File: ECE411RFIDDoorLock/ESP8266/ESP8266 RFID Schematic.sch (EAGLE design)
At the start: 21 parts, among them T1 2N2222, T2 2N2222, X1 ESP-12E

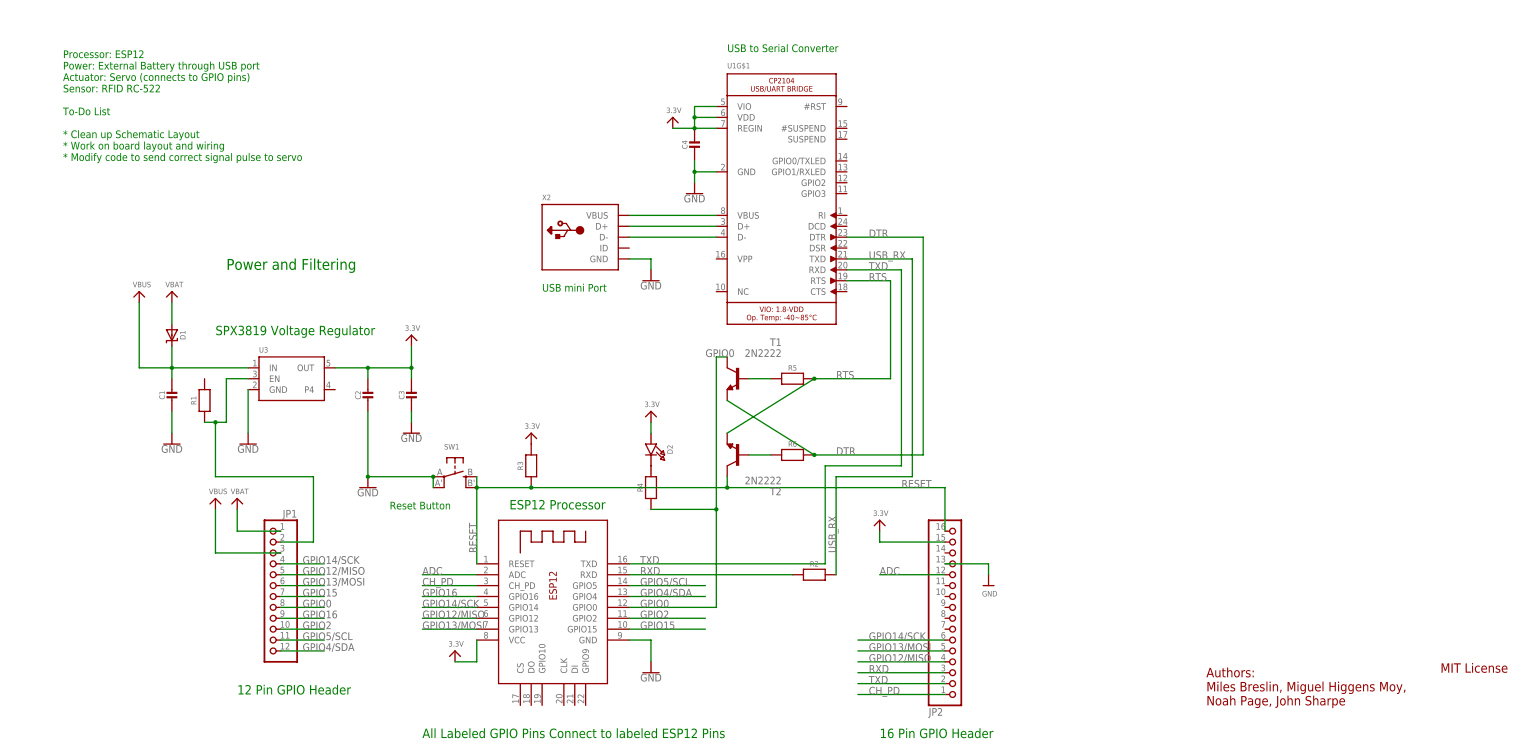
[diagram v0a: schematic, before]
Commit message: Update ESP8266 RFID Schematic.sch
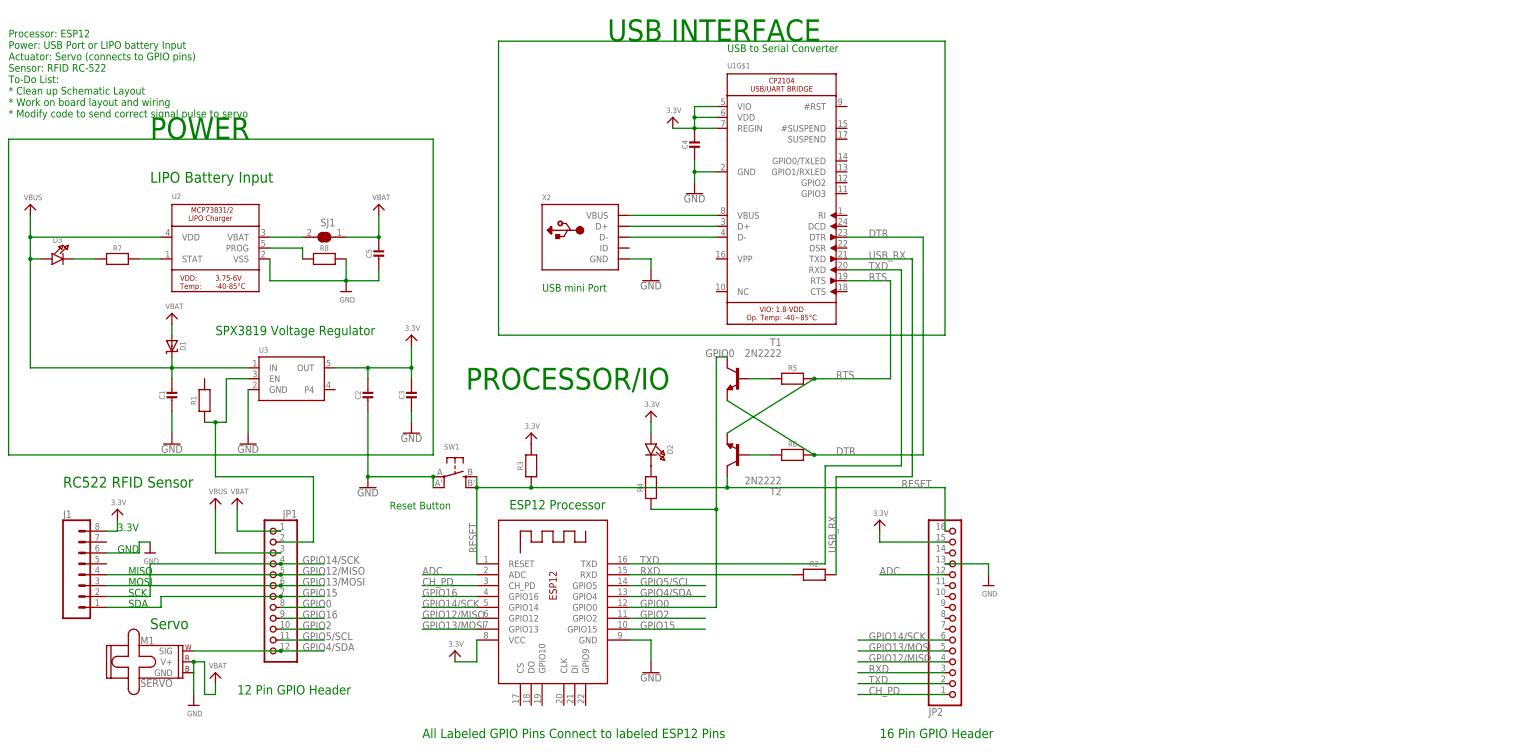
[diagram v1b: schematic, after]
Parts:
- added C5: (no value), microbuilder:CAP_CERAMIC0603MINI
- added D3: (no value), microbuilder:LED0603
- added J1: (no value), SparkFun-Connectors:CONN_08"
- added M1: SERVO, SparkFun-Electromechanical:SERVO
- added R7: (no value), microbuilder:RESISTOR0603MINI
- added R8: (no value), microbuilder:RESISTOR0805_NOOUTLINE
- added SJ1: (no value), microbuilder:SOLDERJUMPER_CLOSED
- added U2: (no value), microbuilder:MCP73831/2
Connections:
- new net N$10: SJ1.2, U2.VBAT
- new net N$11: R8.1, U2.PROG
- new net N$8: D3.C, R7.1
- new net N$9: R7.2, U2.STAT
- net 3.3V: now also J1.8
- net GND: now also C5.2, J1.6, R8.2, U2.VSS
- net GPIO12/MISO: now also J1.4
- net GPIO13/MOSI: now also J1.3
- net GPIO14/SCK: now also J1.2
- net GPIO15: now also J1.1
- net GPIO4/SDA: now also M1.SIG
- net VBAT: now also C5.1, M1.GND, M1.V+, SJ1.1
- net VBUS: now also D3.A, U2.VDD
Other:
- note added: "3.3V"
- note added: "GND"
- note added: "LIPO Battery Input"
- note added: "MISO"
- note added: "MOSI"
- note added: "POWER"
- note added: "PROCESSOR/IO"
- note added: "Processor: ESP12 Power: USB Port or LIPO battery Input Actuator: Servo (connects to GPIO pins) Sensor: RFID RC-522 To-Do List: * Clean up Schematic Layout * Work on board layout and wiring * Modify code to send correct signal pulse to servo"
- note added: "RC522 RFID Sensor"
- note added: "SCK"
- note added: "SDA"
- note added: "Servo"
- note added: "USB INTERFACE"
- note removed: "Authors: Miles Breslin, Miguel Higgens Moy, Noah Page, John Sharpe"
- note removed: "MIT License"
- note removed: "Power and Filtering"
- note removed: "Processor: ESP12 Power: External Battery through USB port Actuator: Servo (connects to GPIO pins) Sensor: RFID RC-522 To-Do List * Clean up Schematic Layout * Work on board layout and wiring * Modify code to send correct signal pulse to servo"
- moved on the sheet: D1

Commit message: First pass at PCB layout
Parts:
- removed C5: (no value), microbuilder:CAP_CERAMIC0603MINI
- removed D1: (no value), microbuilder:DIODE-SCHOTTKYDO-1N4148
- removed D3: (no value), microbuilder:LED0603
- removed JP1: (no value), microbuilder:HEADER-1X12
- removed JP2: (no value), microbuilder:HEADER-1X16
- removed R8: (no value), microbuilder:RESISTOR0805_NOOUTLINE
- removed SJ1: (no value), microbuilder:SOLDERJUMPER_CLOSED
- removed U2: (no value), microbuilder:MCP73831/2
- removed X2: (no value), microbuilder:USBMINIB
- added D4: MBR0540, microbuilder:DIODE-SCHOTTKYSOD-123
- added J2, J3: (no value), SparkFun-Connectors:CONN_02
- added JP4: (no value), microbuilder:HEADER-1X16ROUND
- added JP5: (no value), microbuilder:HEADER-1X12
- added Q3: DMG341, microbuilder:MOSFET-P
- added X4: 20329, microbuilder:USB_MICRO_20329_V2
- C2, C3: value (none) -> 10µF
- R1, R7: value (none) -> 10k
- T1, T2: value 2N2222 -> 600mA/40V; device adafruit:2N2222 -> SparkFun-DiscreteSemi:TRANS_NPN-MMBT2222AL
- U3: value (none) -> AP2112-3.3
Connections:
- removed net N$1: JP1.2, R1.1, U3.EN
- removed net N$11: R8.1, U2.PROG
- removed net OUT: C2.1, C3.1, U3.OUT
- new net EN: JP5.2
- new net N$14: C4.1, U1G$1.VDD, U1G$1.VIO
- net 3.3V: now also C2.1, C3.1, JP4.15, U3.OUT; no longer C4.1, JP2.15, U1G$1.VDD, U1G$1.VIO
- net ADC: now also JP4.12; no longer JP2.12
- net CH_PD: now also JP4.1; no longer JP2.1
- net GND: now also J2.1, J3.1, JP4.13, M1.GND, R7.1, X4.GND; no longer C5.2, JP2.13, R8.2, U2.VSS, X2.GND
- net GPIO0: now also JP5.8; no longer JP1.8
- net GPIO12/MISO: now also JP4.4, JP5.5; no longer JP1.5, JP2.4
- net GPIO13/MOSI: now also JP4.5, JP5.6; no longer JP1.6, JP2.5
- net GPIO14/SCK: now also JP4.6, JP5.4; no longer JP1.4, JP2.6
- net GPIO15: now also JP5.7; no longer JP1.7
- net GPIO16: now also JP5.9; no longer JP1.9
- net GPIO2: now also JP5.10; no longer JP1.10
- net GPIO4/SDA: now also JP5.12; no longer JP1.12
- net GPIO5/SCL: now also J3.2, JP5.11; no longer JP1.11
- net N$10: now also R1.1, U3.EN; no longer SJ1.2, U2.VBAT
- net N$2: now also X4.VBUS; no longer X2.VBUS
- net N$3: now also X4.D+; no longer X2.D+
- net N$4: now also X4.D-; no longer X2.D-
- net N$8: now also C1.1, D4.C, Q3.S, R1.2, U3.IN; no longer D3.C, R7.1
- net N$9: now also D4.A, Q3.G; no longer U2.STAT
- net RESET: now also JP4.16; no longer JP2.16
- net RXD: now also JP4.3; no longer JP2.3
- net TXD: now also JP4.2; no longer JP2.2
- net VBAT: now also J2.2, JP5.1, Q3.D; no longer C5.1, D1.A, JP1.1, M1.GND, SJ1.1
- net VBUS: now also JP5.3; no longer C1.1, D1.C, D3.A, JP1.3, U2.VDD, U3.IN
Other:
- note removed: "12 Pin GPIO Header"
- note removed: "16 Pin GPIO Header"
- note removed: "LIPO Battery Input"
- note removed: "SPX3819 Voltage Regulator"
- note removed: "USB mini Port"
- moved on the sheet: C1, C2, C3, C4, J1, M1, R1, R3, R7, SW1, U3

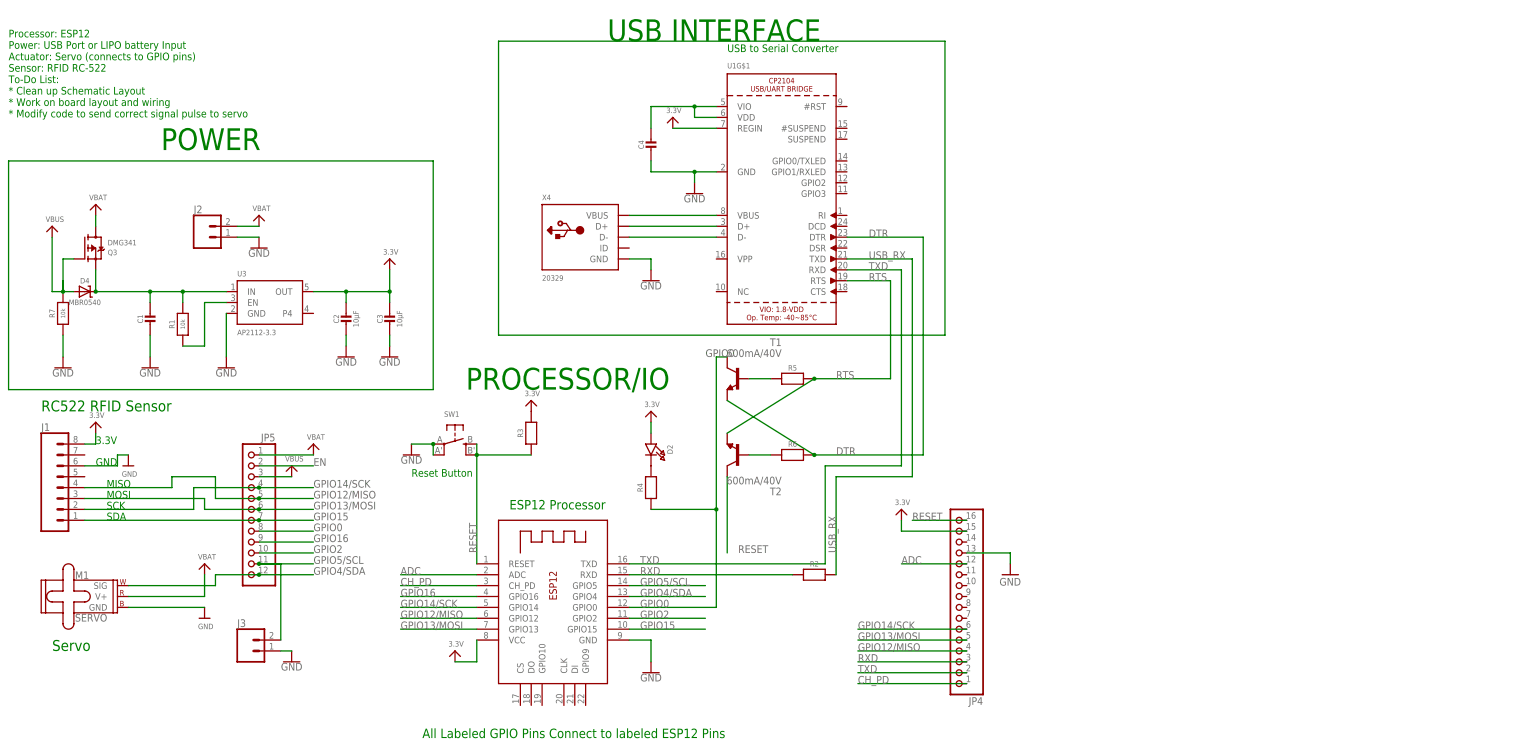
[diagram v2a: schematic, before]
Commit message: Added some missing component values
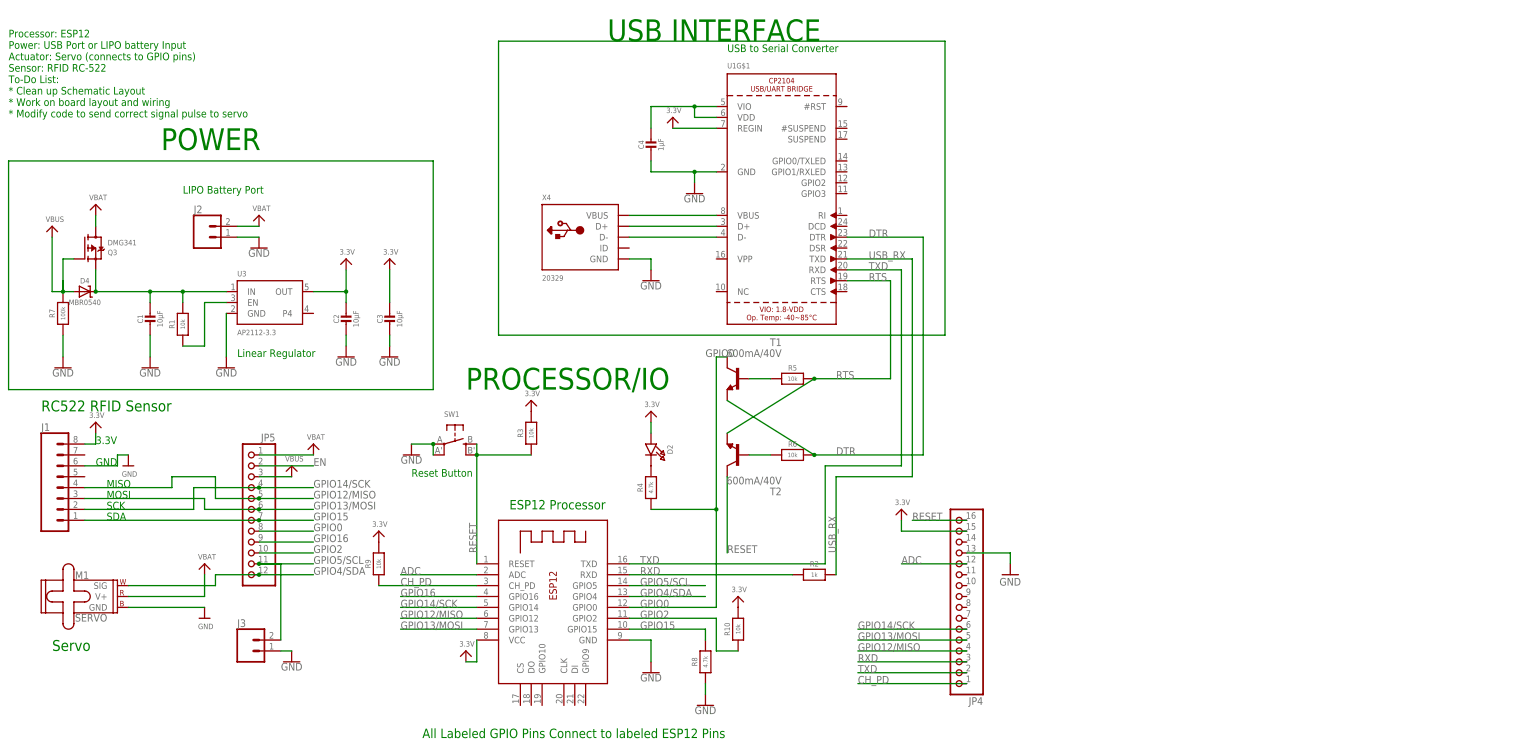
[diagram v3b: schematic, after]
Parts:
- added R10, R9: 10k, microbuilder:RESISTOR0603MINI
- added R8: 4.7k, microbuilder:RESISTOR0603MINI
- C1: value (none) -> 10µF
- C4: value (none) -> 1µF
- R2: value (none) -> 1k
- R3, R5, R6: value (none) -> 10k
- R4: value (none) -> 4.7k
- R7: value 10k -> 100k
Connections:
- net 3.3V: now also R10.2, R9.2
- net CH_PD: now also R9.1
- net GND: now also R8.1
- net GPIO15: now also R8.2
- net GPIO2: now also R10.1
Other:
- note added: "LIPO Battery Port"
- note added: "Linear Regulator"
